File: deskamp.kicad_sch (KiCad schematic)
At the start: 24 parts, among them J1 Input 01, J2 Input 02, J3 Preamp Out, J4 Selector Switch, J5 LFE, J6 Mute, J7 Sleep, J8 Motor, K1 Mute, K2 Sleep, K3 TQ2-12V, K4 TQ2-12V, U1 esp32-wemos-d1-mini, U2 L9110, U3 LM2575-3.3BT

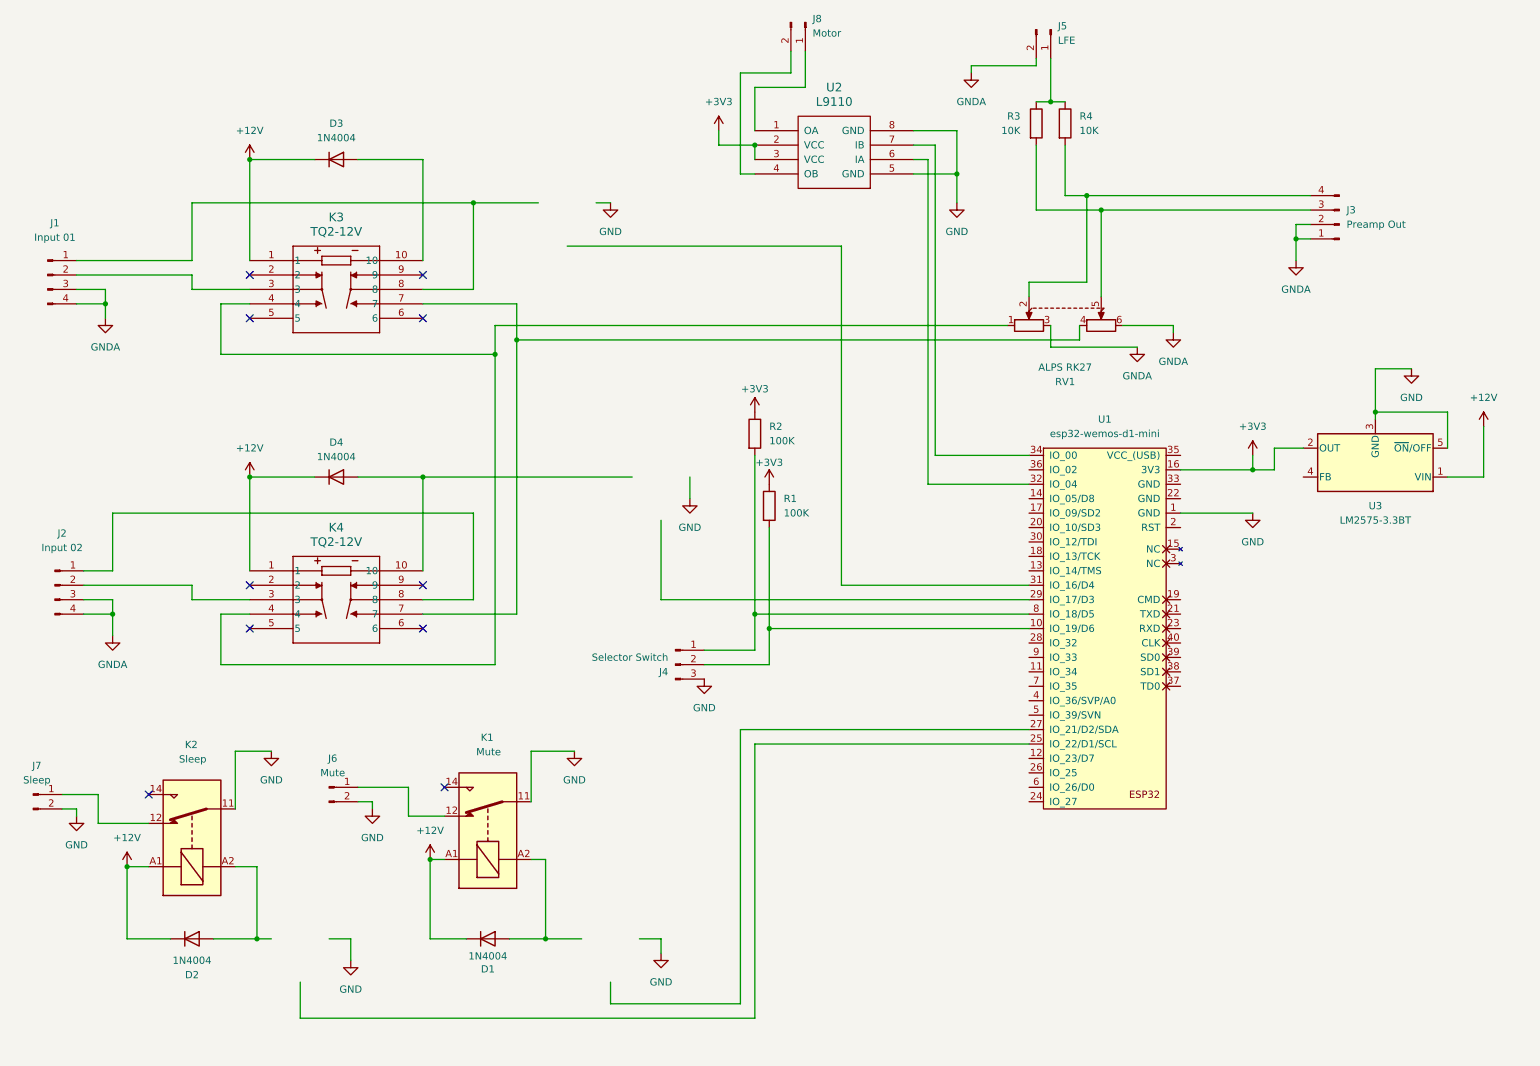
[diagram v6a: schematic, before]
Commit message: Add transistors, start building PCB
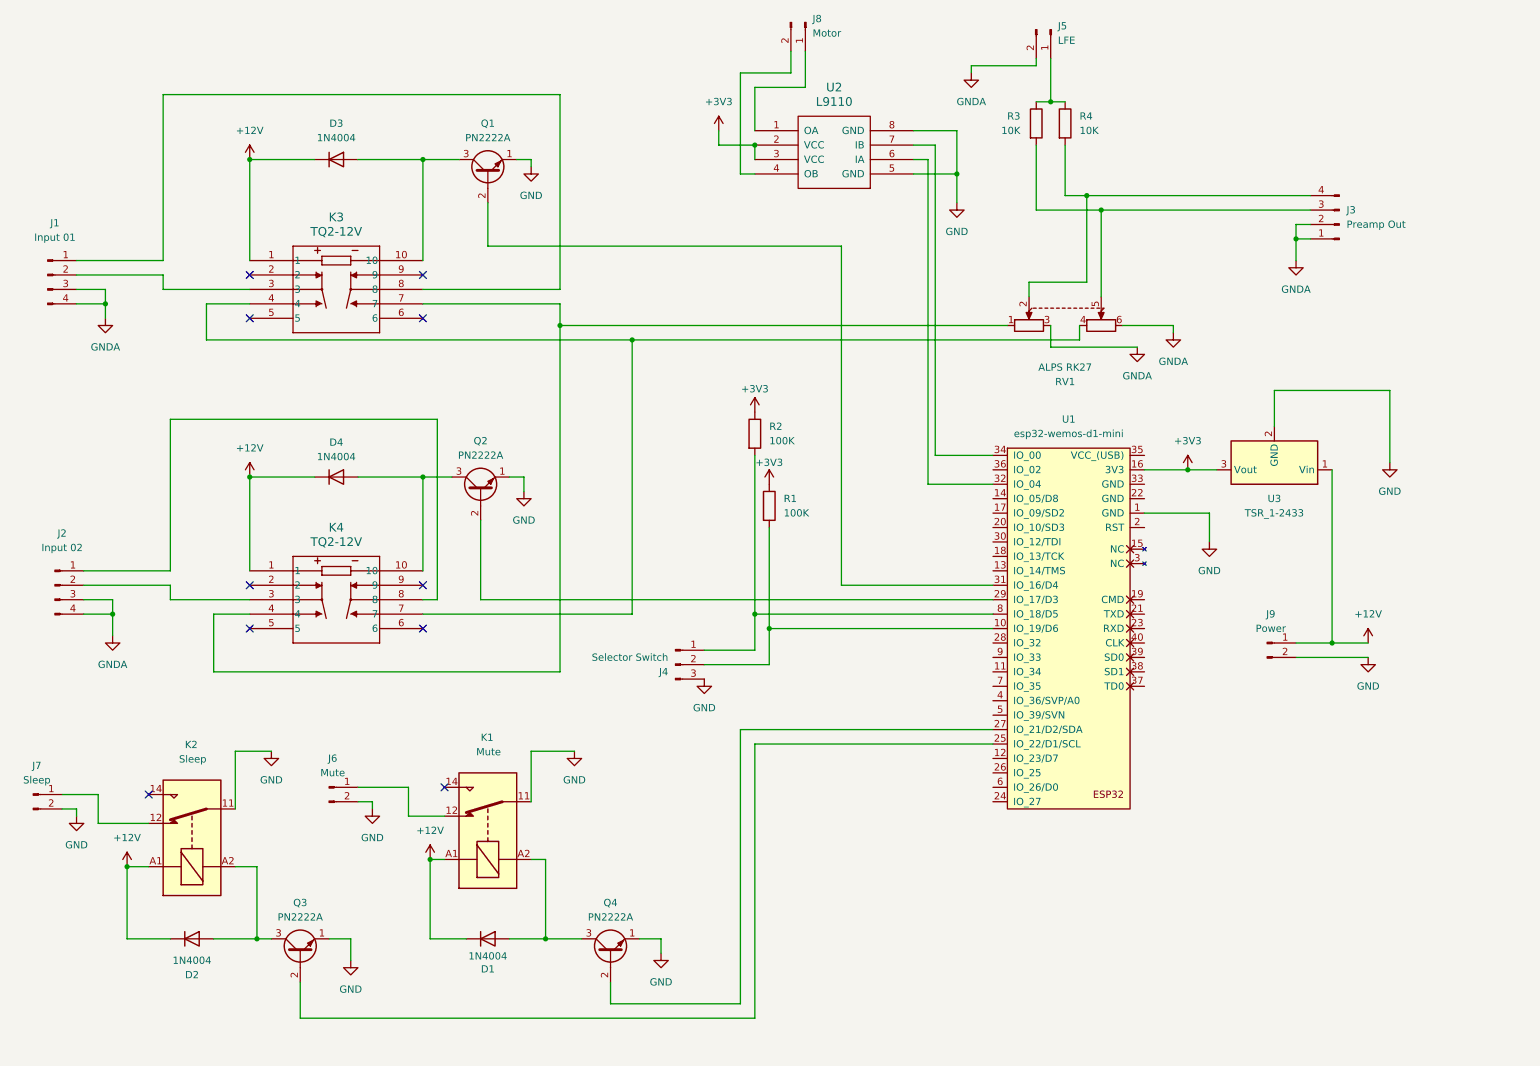
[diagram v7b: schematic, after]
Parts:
- removed U3: LM2575-3.3BT, Package_TO_SOT_THT:TO-220-5_Vertical, symbol Regulator_Switching:LM2575-3.3BT
- added J9: Power, Connector_JST:JST_XH_B2B-XH-AM_1x02_P2.50mm_Vertical, symbol Connector:Conn_01x02_Pin
- added Q1, Q2, Q3, Q4: PN2222A, Package_TO_SOT_THT:TO-92L_HandSolder, symbol Transistor_BJT:PN2222A
- added U3: TSR_1-2433, tsr-2433:TSR1-SINGLE_TRP, symbol Regulator_Switching:TSR_1-2433
- J4: footprint (none) -> Connector_JST:JST_XH_B3B-XH-AM_1x03_P2.50mm_Vertical
- J6, J7: footprint (none) -> Connector_JST:JST_XH_B2B-XH-A_1x02_P2.50mm_Vertical
- J8: footprint (none) -> Connector_JST:JST_XH_B2B-XH-AM_1x02_P2.50mm_Vertical
- K3, K4: footprint RELAY_TQ2_PAN -> tq2:RELAY_TQ2_PAN
- U2: footprint (none) -> L9110:so-8
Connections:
- net +12V: now also J9.1 (Pin_1), U3.1 (Vin)
- net +3V3: now also U3.3 (Vout)
- net GND: now also J9.2 (Pin_2), Q1.1 (E), Q2.1 (E), Q3.1 (E), Q4.1 (E), U3.2 (GND)
- net at D1.2 (A), K1.A2: now also Q4.3 (C)
- net at D4.2 (A), K4.10: now also Q2.3 (C)
- net at D2.2 (A), K2.A2: now also Q3.3 (C)
- net at D3.2 (A), K3.10: now also Q1.3 (C)
- net at K4.4, RV1.1: now also K3.7; no longer K3.4
- net at K4.7, RV1.4: now also K3.4; no longer K3.7
- net at U1.25 (IO_22/D1/SCL): now also Q3.2 (B)
- net at U1.27 (IO_21/D2/SDA): now also Q4.2 (B)
- net at U1.29 (IO_17/D3): now also Q2.2 (B)
- net at U1.31 (IO_16/D4): now also Q1.2 (B)
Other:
- moved on the sheet: U1

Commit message: Stuck until modelling Alps pot
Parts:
- removed K1: Mute, Relay_THT:Relay_SPDT_Panasonic_JW1_FormC, symbol Relay:Relay_SPDT
- removed K2: Sleep, Relay_THT:Relay_SPDT_Panasonic_JW1_FormC, symbol Relay:Relay_SPDT
- added K1, K2: TQ2-12V, tq2:RELAY_TQ2_PAN, symbol 2025-10-05_02-56-43:TQ2-12V
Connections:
- net +12V: now also K1.1, K2.1
- net GND: now also K1.3, K2.3
- net at Q3.2 (B): now also U1.27 (IO_21/D2/SDA); no longer U1.25 (IO_22/D1/SCL)
- net at D2.2 (A), Q3.3 (C): now also K2.10
- net at J6.1 (Pin_1): now also K1.4
- net at D1.2 (A), Q4.3 (C): now also K1.10
- net at J7.1 (Pin_1): now also K2.2
- net at Q4.2 (B): now also U1.25 (IO_22/D1/SCL); no longer U1.27 (IO_21/D2/SDA)
- no-connect marks 10 -> 8
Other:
- moved on the sheet: D1, D2, J6, J7, Q3, Q4
